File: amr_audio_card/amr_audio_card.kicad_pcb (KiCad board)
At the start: 2 copper layers, 68.8 x 63.9 mm, 3 parts, among them J1 Conn_Coaxial, J2 USB_A, U1 Bus_AMR

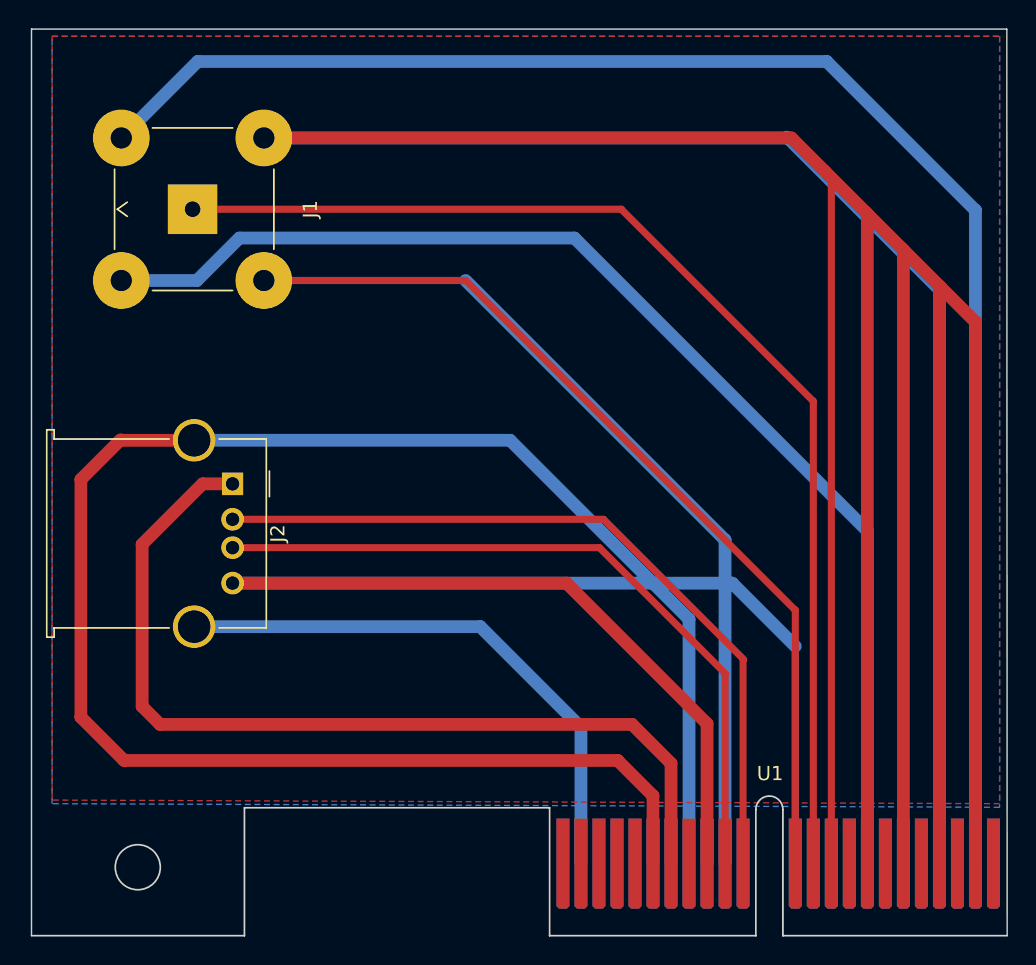
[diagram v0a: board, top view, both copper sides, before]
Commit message: remove empty corner
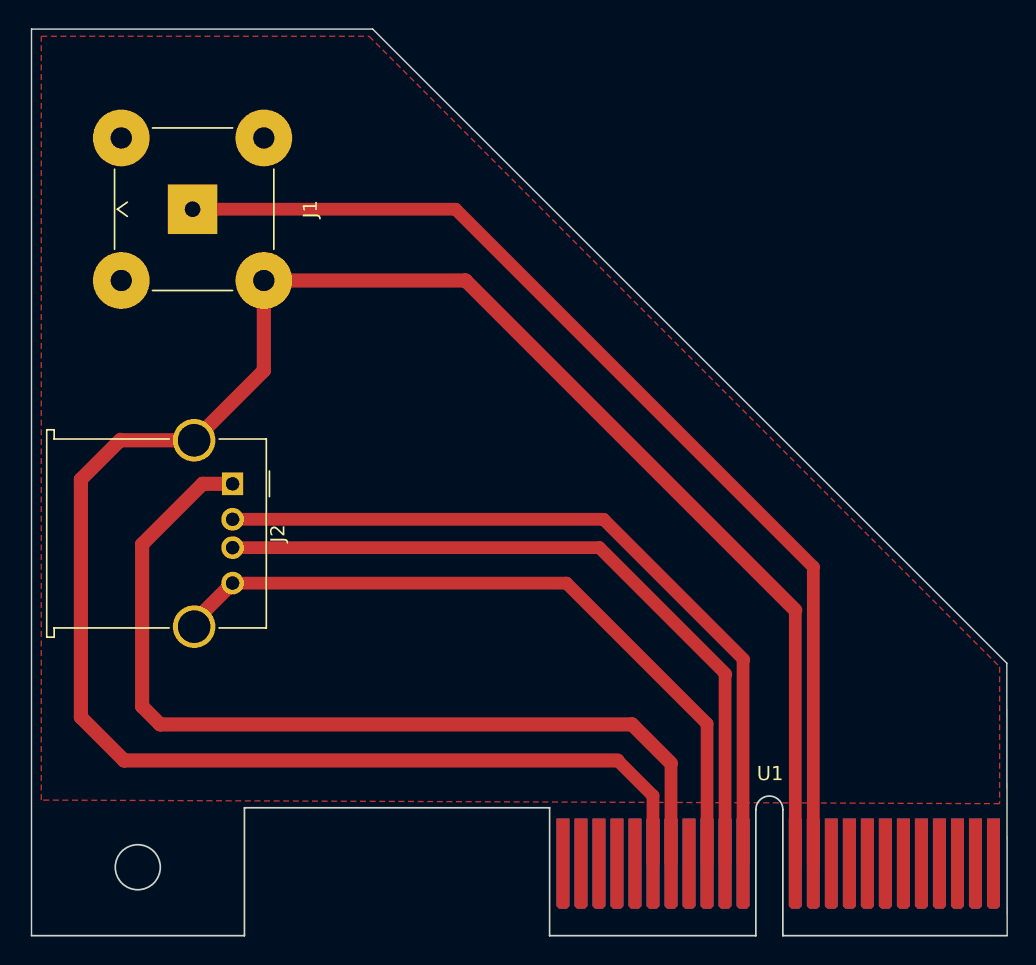
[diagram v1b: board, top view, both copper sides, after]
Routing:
- net GND: track 966.6 -> 203.2 mm
- net Net-(J1-Pad1): track 82.0 -> 75.1 mm
- removed copper zone on B.Cu, net GND
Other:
- outline, holes or cut-outs redrawn

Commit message: update pcb
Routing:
- net GND: track 203.2 -> 292.5 mm
- net Net-(J1-Pad1): track 75.1 -> 68.0 mm
- net Net-(J2-Pad2): track 54.5 -> 50.0 mm
- net Net-(J2-Pad3): track 51.9 -> 47.5 mm
- net Net-(J2-Pad1): track 65.6 -> 67.4 mm
- added copper zone on B.Cu, net GND
- removed copper zone on F.Cu, net GND
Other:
- board text added: "DIGITAL AUDIO"
- board text added: "USB"

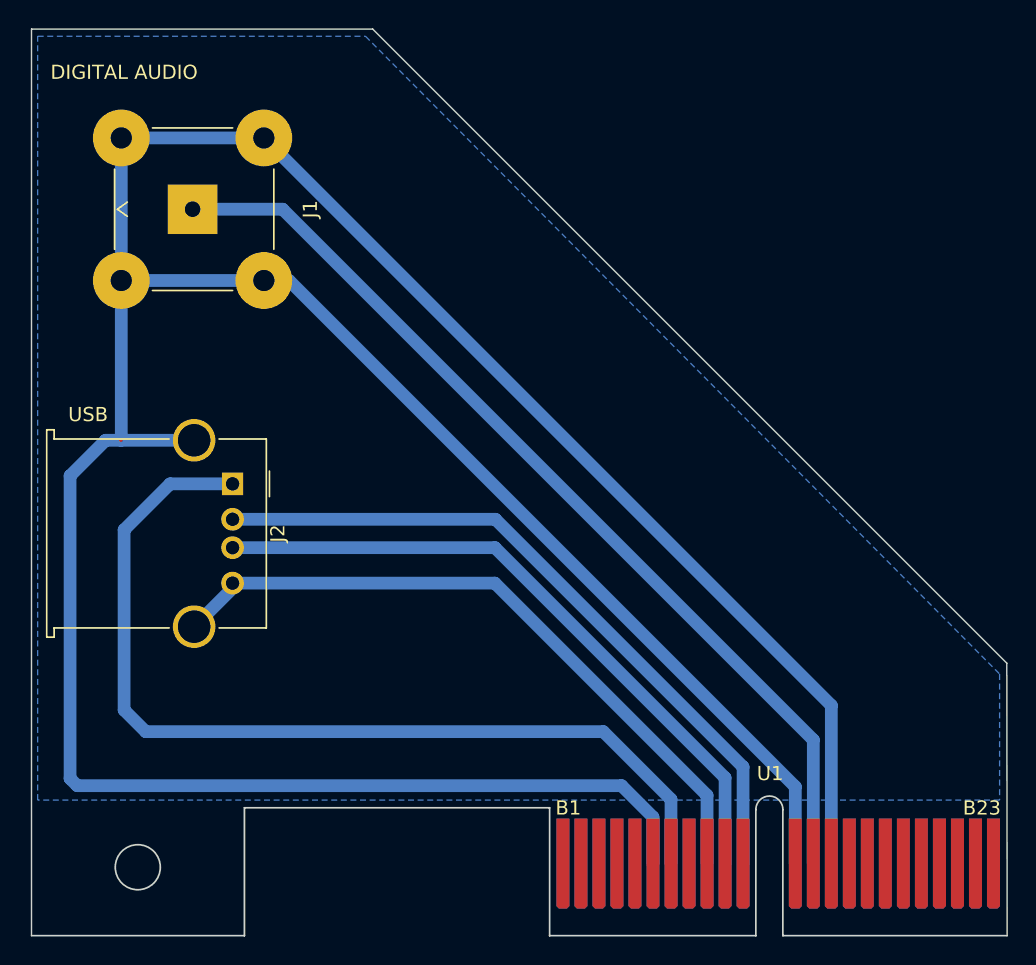
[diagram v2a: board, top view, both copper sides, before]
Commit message: add an actual RCA jack
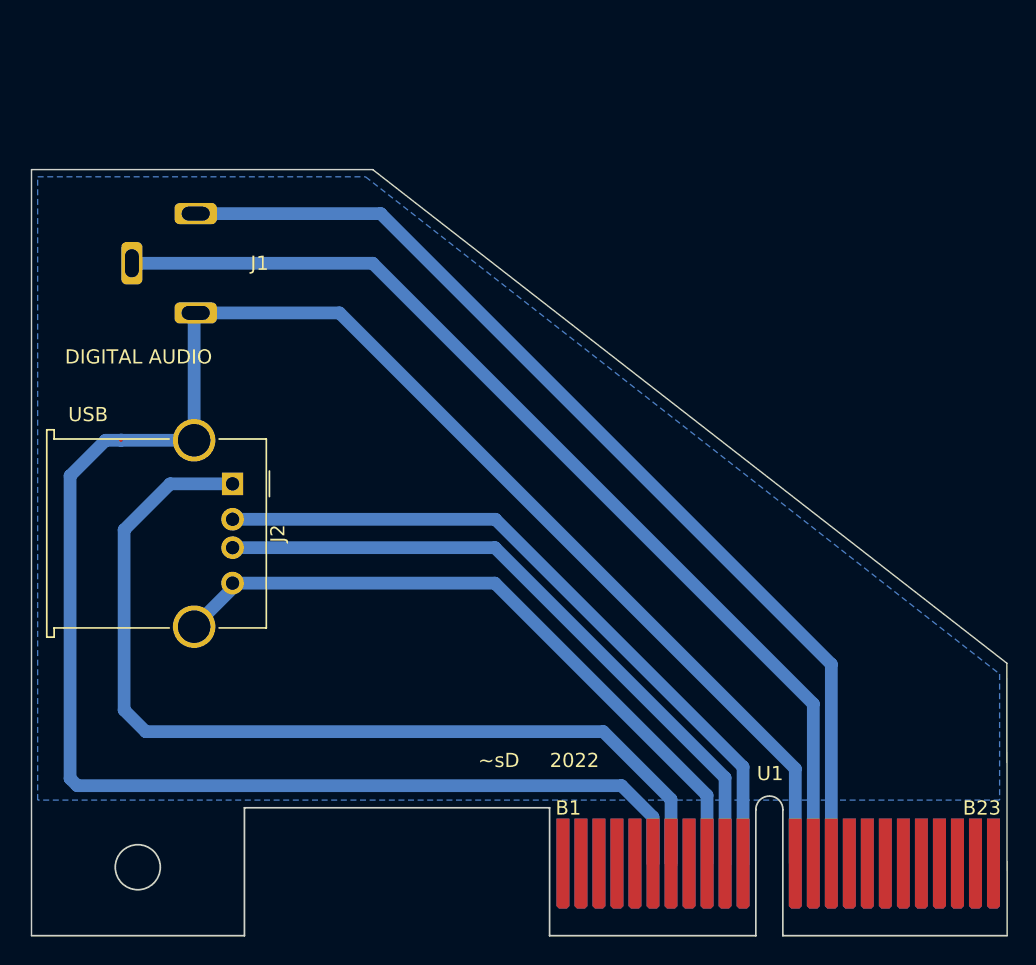
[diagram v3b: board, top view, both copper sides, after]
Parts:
- J1: footprint Connector_Coaxial:BNC_TEConnectivity_1478035_Horizontal -> Bus-Connector:Cinch
- moved J1 4.20 mm to (102.4, 115.6), turned to 0 degrees
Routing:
- net GND: track 292.5 -> 269.0 mm
- net Net-(J1-Pad1): track 68.0 -> 72.2 mm
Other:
- board size 68.8 x 63.9 mm -> 68.8 x 54 mm
- board text added: "2022"
- board text added: "~sD"
